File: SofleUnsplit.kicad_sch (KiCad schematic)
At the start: 117 parts, among them SW1 Switch, SW10 Switch, SW11 Switch, SW12 Switch, SW13 Switch, SW14 Switch, SW15 Switch, SW16 Switch, SW17 Switch, SW18 Switch, SW19 Switch, SW2 Switch, SW20 Switch, SW21 Switch, SW22 Switch, SW23 Switch, SW24 Switch, SW25 Switch, SW26 Switch, SW27 Switch, SW28 Switch, SW29 Switch, SW3 Switch, SW30 Switch, SW31 Switch, SW32 Switch, SW33 Switch, SW34 Switch, SW35 Switch, SW36 Switch, SW37 Switch, SW38 Switch, SW39 Switch, SW4 Switch, SW40 Switch, SW41 Switch, SW42 Switch, SW43 Switch, SW44 Switch, SW45 Switch, SW46 Switch, SW47 Switch, SW48 Switch, SW49 Switch, SW5 Switch, SW50 Switch, SW51 Switch, SW52 Switch, SW53 Switch, SW54 Switch, SW55 Switch, SW56 Switch, SW57 Switch, SW58 Switch, SW6 Switch, SW7 Switch, SW8 Switch, SW9 Switch, U1 MCU_rp2040-zero

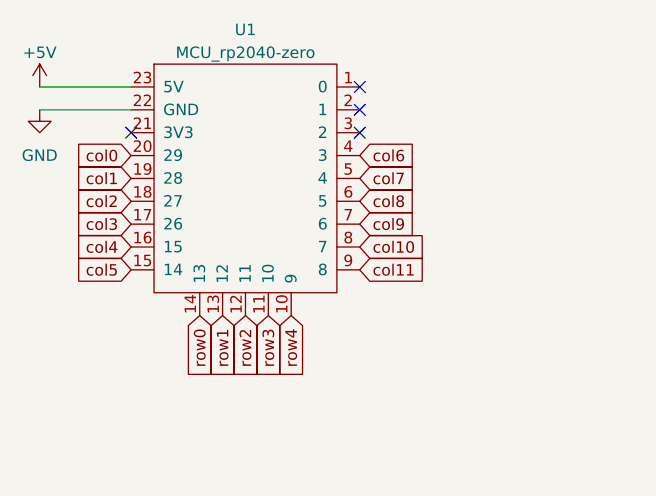
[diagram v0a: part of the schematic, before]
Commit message: Place diodes differently
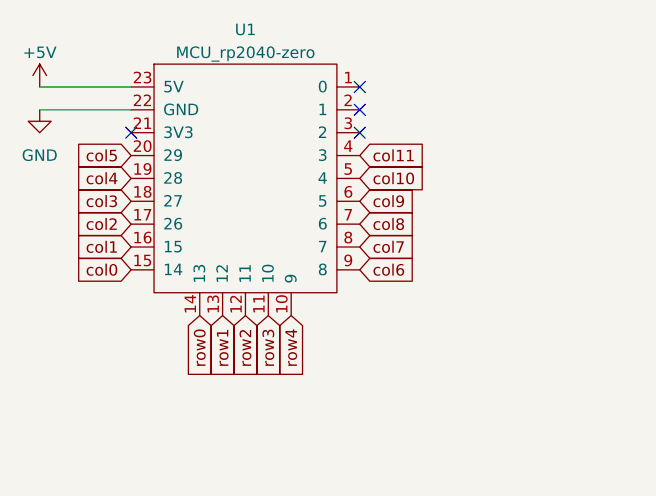
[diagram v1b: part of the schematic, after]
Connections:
- net col0: now also U1.15 (14); no longer U1.20 (29)
- net col1: now also U1.16 (15); no longer U1.19 (28)
- net col10: now also U1.5 (4); no longer U1.8 (7)
- net col11: now also U1.4 (3); no longer U1.9 (8)
- net col2: now also U1.17 (26); no longer U1.18 (27)
- net col3: now also U1.18 (27); no longer U1.17 (26)
- net col4: now also U1.19 (28); no longer U1.16 (15)
- net col5: now also U1.20 (29); no longer U1.15 (14)
- net col6: now also U1.9 (8); no longer U1.4 (3)
- net col7: now also U1.8 (7); no longer U1.5 (4)
- net col8: now also U1.7 (6); no longer U1.6 (5)
- net col9: now also U1.6 (5); no longer U1.7 (6)
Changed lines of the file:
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@@
     (stroke (width 0) (type default))
   )
-  (global_label "col8" (shape input) (at 66.04 55.88 0) (fields_autoplaced)
+  (global_label "col8" (shape input) (at 66.04 58.42 0) (fields_autoplaced)
     (effects (font (size 1.27 1.27)) (justify left))
-    (property "Intersheetrefs" "${INTERSHEET_REFS}" (at 73.0581 55.88 0)
+    (property "Intersheetrefs" "${INTERSHEET_REFS}" (at 73.0581 58.42 0)
       (effects (font (size 1.27 1.27)) (justify left) hide)
     )
@@
     )
   )
-  (global_label "col4" (shape input) (at 40.64 60.96 180) (fields_autoplaced)
+  (global_label "col4" (shape input) (at 40.64 53.34 180) (fields_autoplaced)
     (effects (font (size 1.27 1.27)) (justify right))
-    (property "Intersheetrefs" "${INTERSHEET_REFS}" (at 33.6219 60.96 0)
+    (property "Intersheetrefs" "${INTERSHEET_REFS}" (at 33.6219 53.34 0)
       (effects (font (size 1.27 1.27)) (justify right) hide)
     )
@@
     )
   )
-  (global_label "col9" (shape input) (at 66.04 58.42 0) (fields_autoplaced)
+  (global_label "col9" (shape input) (at 66.04 55.88 0) (fields_autoplaced)
     (effects (font (size 1.27 1.27)) (justify left))
-    (property "Intersheetrefs" "${INTERSHEET_REFS}" (at 73.0581 58.42 0)
+    (property "Intersheetrefs" "${INTERSHEET_REFS}" (at 73.0581 55.88 0)
       (effects (font (size 1.27 1.27)) (justify left) hide)
     )
   )
-  (global_label "col10" (shape input) (at 66.04 60.96 0) (fields_autoplaced)
+  (global_label "col10" (shape input) (at 66.04 53.34 0) (fields_autoplaced)
     (effects (font (size 1.27 1.27)) (justify left))
-    (property "Intersheetrefs" "${INTERSHEET_REFS}" (at 73.0581 60.96 0)
+    (property "Intersheetrefs" "${INTERSHEET_REFS}" (at 73.0581 53.34 0)
       (effects (font (size 1.27 1.27)) (justify left) hide)
     )
@@
     )
   )
-  (global_label "col2" (shape input) (at 40.64 55.88 180) (fields_autoplaced)
+  (global_label "col2" (shape input) (at 40.64 58.42 180) (fields_autoplaced)
+    (effects (font (size 1.27 1.27)) (justify right))
+    (property "Intersheetrefs" "${INTERSHEET_REFS}" (at 33.6219 58.42 0)
+      (effects (font (size 1.27 1.27)) (justify right) hide)
+    )
+  )
+  (global_label "col3" (shape input) (at 40.64 55.88 180) (fields_autoplaced)
     (effects (font (size 1.27 1.27)) (justify right))
     (property "Intersheetrefs" "${INTERSHEET_REFS}" (at 33.6219 55.88 0)
@@
     )
   )
-  (global_label "col3" (shape input) (at 40.64 58.42 180) (fields_autoplaced)
+  (global_label "col1" (shape input) (at 40.64 60.96 180) (fields_autoplaced)
     (effects (font (size 1.27 1.27)) (justify right))
-    (property "Intersheetrefs" "${INTERSHEET_REFS}" (at 33.6219 58.42 0)
-      (effects (font (size 1.27 1.27)) (justify right) hide)
-    )
-  )
-  (global_label "col1" (shape input) (at 40.64 53.34 180) (fields_autoplaced)
-    (effects (font (size 1.27 1.27)) (justify right))
-    (property "Intersheetrefs" "${INTERSHEET_REFS}" (at 33.6219 53.34 0)
+    (property "Intersheetrefs" "${INTERSHEET_REFS}" (at 33.6219 60.96 0)
       (effects (font (size 1.27 1.27)) (justify right) hide)
     )
@@
     )
   )
-  (global_label "col0" (shape input) (at 40.64 50.8 180) (fields_autoplaced)
+  (global_label "col0" (shape input) (at 40.64 63.5 180) (fields_autoplaced)
+    (effects (font (size 1.27 1.27)) (justify right))
+    (property "Intersheetrefs" "${INTERSHEET_REFS}" (at 33.6219 63.5 0)
+      (effects (font (size 1.27 1.27)) (justify right) hide)
+    )
+  )
+  (global_label "col5" (shape input) (at 40.64 50.8 180) (fields_autoplaced)
     (effects (font (size 1.27 1.27)) (justify right))
     (property "Intersheetrefs" "${INTERSHEET_REFS}" (at 33.6219 50.8 0)
@@
     )
   )
-  (global_label "col5" (shape input) (at 40.64 63.5 180) (fields_autoplaced)
-    (effects (font (size 1.27 1.27)) (justify right))
-    (property "Intersheetrefs" "${INTERSHEET_REFS}" (at 33.6219 63.5 0)
-      (effects (font (size 1.27 1.27)) (justify right) hide)
-    )
-  )
-  (global_label "col11" (shape input) (at 66.04 63.5 0) (fields_autoplaced)
+  (global_label "col11" (shape input) (at 66.04 50.8 0) (fields_autoplaced)
     (effects (font (size 1.27 1.27)) (justify left))
-    (property "Intersheetrefs" "${INTERSHEET_REFS}" (at 73.0581 63.5 0)
+    (property "Intersheetrefs" "${INTERSHEET_REFS}" (at 73.0581 50.8 0)
       (effects (font (size 1.27 1.27)) (justify left) hide)
     )
@@
     )
   )
-  (global_label "col6" (shape input) (at 66.04 50.8 0)
+  (global_label "col6" (shape input) (at 66.04 63.5 0)
     (effects (font (size 1.27 1.27)) (justify left))
-    (property "Intersheetrefs" "${INTERSHEET_REFS}" (at 73.0581 50.8 0)
+    (property "Intersheetrefs" "${INTERSHEET_REFS}" (at 73.0581 63.5 0)
       (effects (font (size 1.27 1.27)) (justify left) hide)
     )
@@
     )
   )
-  (global_label "col7" (shape input) (at 66.04 53.34 0) (fields_autoplaced)
+  (global_label "col7" (shape input) (at 66.04 60.96 0) (fields_autoplaced)
     (effects (font (size 1.27 1.27)) (justify left))
-    (property "Intersheetrefs" "${INTERSHEET_REFS}" (at 73.0581 53.34 0)
+    (property "Intersheetrefs" "${INTERSHEET_REFS}" (at 73.0581 60.96 0)
       (effects (font (size 1.27 1.27)) (justify left) hide)
     )

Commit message: Routing done
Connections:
- net col0: now also U1.20 (29); no longer U1.15 (14)
- net col1: now also U1.19 (28); no longer U1.16 (15)
- net col2: now also U1.18 (27); no longer U1.17 (26)
- net col3: now also U1.17 (26); no longer U1.18 (27)
- net col4: now also U1.16 (15); no longer U1.19 (28)
- net col5: now also U1.15 (14); no longer U1.20 (29)
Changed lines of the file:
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@@
     )
   )
-  (global_label "col4" (shape input) (at 40.64 53.34 180) (fields_autoplaced)
+  (global_label "col4" (shape input) (at 40.64 60.96 180) (fields_autoplaced)
     (effects (font (size 1.27 1.27)) (justify right))
-    (property "Intersheetrefs" "${INTERSHEET_REFS}" (at 33.6219 53.34 0)
+    (property "Intersheetrefs" "${INTERSHEET_REFS}" (at 33.6219 60.96 0)
       (effects (font (size 1.27 1.27)) (justify right) hide)
     )
@@
     )
   )
-  (global_label "col2" (shape input) (at 40.64 58.42 180) (fields_autoplaced)
+  (global_label "col2" (shape input) (at 40.64 55.88 180) (fields_autoplaced)
+    (effects (font (size 1.27 1.27)) (justify right))
+    (property "Intersheetrefs" "${INTERSHEET_REFS}" (at 33.6219 55.88 0)
+      (effects (font (size 1.27 1.27)) (justify right) hide)
+    )
+  )
+  (global_label "col3" (shape input) (at 40.64 58.42 180) (fields_autoplaced)
     (effects (font (size 1.27 1.27)) (justify right))
     (property "Intersheetrefs" "${INTERSHEET_REFS}" (at 33.6219 58.42 0)
@@
     )
   )
-  (global_label "col3" (shape input) (at 40.64 55.88 180) (fields_autoplaced)
+  (global_label "col1" (shape input) (at 40.64 53.34 180) (fields_autoplaced)
     (effects (font (size 1.27 1.27)) (justify right))
-    (property "Intersheetrefs" "${INTERSHEET_REFS}" (at 33.6219 55.88 0)
-      (effects (font (size 1.27 1.27)) (justify right) hide)
-    )
-  )
-  (global_label "col1" (shape input) (at 40.64 60.96 180) (fields_autoplaced)
-    (effects (font (size 1.27 1.27)) (justify right))
-    (property "Intersheetrefs" "${INTERSHEET_REFS}" (at 33.6219 60.96 0)
+    (property "Intersheetrefs" "${INTERSHEET_REFS}" (at 33.6219 53.34 0)
       (effects (font (size 1.27 1.27)) (justify right) hide)
     )
@@
     )
   )
-  (global_label "col0" (shape input) (at 40.64 63.5 180) (fields_autoplaced)
+  (global_label "col0" (shape input) (at 40.64 50.8 180) (fields_autoplaced)
+    (effects (font (size 1.27 1.27)) (justify right))
+    (property "Intersheetrefs" "${INTERSHEET_REFS}" (at 33.6219 50.8 0)
+      (effects (font (size 1.27 1.27)) (justify right) hide)
+    )
+  )
+  (global_label "col5" (shape input) (at 40.64 63.5 180) (fields_autoplaced)
     (effects (font (size 1.27 1.27)) (justify right))
     (property "Intersheetrefs" "${INTERSHEET_REFS}" (at 33.6219 63.5 0)
       (effects (font (size 1.27 1.27)) (justify right) hide)
     )
-  )
-  (global_label "col5" (shape input) (at 40.64 50.8 180) (fields_autoplaced)
-    (effects (font (size 1.27 1.27)) (justify right))
-    (property "Intersheetrefs" "${INTERSHEET_REFS}" (at 33.6219 50.8 0)
-      (effects (font (size 1.27 1.27)) (justify right) hide)
-    )

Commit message: Polishing, finishing
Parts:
- added J1: Conn_01x04, Connector_PinSocket_2.54mm:PinSocket_1x04_P2.54mm_Vertical, symbol Connector_Generic:Conn_01x04
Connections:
- net +5V: now also J1.1 (Pin_1)
- net GND: now also J1.4 (Pin_4)
- net SDA: now reaches U1.1 (0)
- net SDA: now also J1.3 (Pin_3)
- net SCL: now reaches U1.2 (1)
- net SCL: now also J1.2 (Pin_2)
- no-connect marks 4 -> 2
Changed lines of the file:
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@@
   (junction (at 326.39 191.77) (diameter 0) (color 0 0 0 0)
   )
-  (no_connect (at 66.04 43.18))
   (no_connect (at 40.64 48.26))
   (no_connect (at 66.04 48.26))
-  (no_connect (at 66.04 45.72))
   (wire (pts (xy 43.18 208.28) (xy 67.31 208.28))
     (stroke (width 0) (type default))
@@
     (stroke (width 0) (type default))
   )
+  (wire (pts (xy 113.03 41.91) (xy 121.92 41.91))
+    (stroke (width 0) (type default))
+  )
   (wire (pts (xy 96.52 208.28) (xy 124.46 208.28))
     (stroke (width 0) (type default))
@@
     (stroke (width 0) (type default))
   )
+  (wire (pts (xy 113.03 49.53) (xy 125.73 49.53))
+    (stroke (width 0) (type default))
+  )
   (wire (pts (xy 251.46 167.64) (xy 251.46 184.15))
     (stroke (width 0) (type default))
@@
     )
   )
+  (global_label "SCL" (shape input) (at 66.04 45.72 0) (fields_autoplaced)
+    (effects (font (size 1.27 1.27)) (justify left))
+    (property "Intersheetrefs" "${INTERSHEET_REFS}" (at 72.4534 45.72 0)
+      (effects (font (size 1.27 1.27)) (justify left) hide)
+    )
+  )
   (global_label "col4" (shape input) (at 166.37 157.48 90) (fields_autoplaced)
     (effects (font (size 1.27 1.27)) (justify left))
@@
     )
   )
+  (global_label "SDA" (shape input) (at 66.04 43.18 0) (fields_autoplaced)
+    (effects (font (size 1.27 1.27)) (justify left))
+    (property "Intersheetrefs" "${INTERSHEET_REFS}" (at 72.5139 43.18 0)
+      (effects (font (size 1.27 1.27)) (justify left) hide)
+    )
+  )
   (global_label "col5" (shape input) (at 195.58 157.48 90) (fields_autoplaced)
     (effects (font (size 1.27 1.27)) (justify left))
@@
     )
   )
+  (global_label "SDA" (shape input) (at 113.03 44.45 0) (fields_autoplaced)
+    (effects (font (size 1.27 1.27)) (justify left))
+    (property "Intersheetrefs" "${INTERSHEET_REFS}" (at 119.5039 44.45 0)
+      (effects (font (size 1.27 1.27)) (justify left) hide)
+    )
+  )
+  (global_label "SCL" (shape input) (at 113.03 46.99 0) (fields_autoplaced)
+    (effects (font (size 1.27 1.27)) (justify left))
+    (property "Intersheetrefs" "${INTERSHEET_REFS}" (at 119.4434 46.99 0)
+      (effects (font (size 1.27 1.27)) (justify left) hide)
+    )
+  )
   (global_label "col1" (shape input) (at 81.28 157.48 90) (fields_autoplaced)
     (effects (font (size 1.27 1.27)) (justify left))
@@
     )
   )
+  (symbol (lib_id "power:+5V") (at 125.73 49.53 0) (unit 1)
+    (in_bom yes) (on_board yes) (dnp no) (fields_autoplaced)
+    (property "Reference" "#PWR03" (at 125.73 53.34 0)
+      (effects (font (size 1.27 1.27)) hide)
+    )
+    (property "Value" "+5V" (at 125.73 45.72 0)
+      (effects (font (size 1.27 1.27)))
+    )
+    (property "Footprint" "" (at 125.73 49.53 0)
+      (effects (font (size 1.27 1.27)) hide)
+    )
+    (property "Datasheet" "" (at 125.73 49.53 0)
+      (effects (font (size 1.27 1.27)) hide)
+    )
+    (pin "1")
+    (instances
+      (project "SofleUnsplit"
+        (path "/0271784e-2195-481b-b0c9-914478a67f87"
+          (reference "#PWR03") (unit 1)
+        )
+      )
+    )
+  )
   (symbol (lib_id "Diode:1N4148W") (at 326.39 220.98 90) (unit 1)
     (in_bom yes) (on_board yes) (dnp no) (fields_autoplaced)
@@
     )
   )
+  (symbol (lib_id "Connector_Generic:Conn_01x04") (at 107.95 46.99 180) (unit 1)
+    (in_bom yes) (on_board yes) (dnp no) (fields_autoplaced)
+    (property "Reference" "J1" (at 107.95 36.83 0)
+      (effects (font (size 1.27 1.27)))
+    )
+    (property "Value" "Conn_01x04" (at 107.95 39.37 0)
+      (effects (font (size 1.27 1.27)))
+    )
+    (property "Footprint" "Connector_PinSocket_2.54mm:PinSocket_1x04_P2.54mm_Vertical" (at 107.95 46.99 0)
+      (effects (font (size 1.27 1.27)) hide)
+    )
+    (property "Datasheet" "~" (at 107.95 46.99 0)
+      (effects (font (size 1.27 1.27)) hide)
+    )
+    (pin "1")
+    (pin "2")
+    (pin "3")
+    (pin "4")
+    (instances
+      (project "SofleUnsplit"
+        (path "/0271784e-2195-481b-b0c9-914478a67f87"
+          (reference "J1") (unit 1)
+        )
+      )
+    )
+  )
   (symbol (lib_id "zzkeeb:Switch") (at 144.78 200.66 0) (unit 1)
     (in_bom yes) (on_board yes) (dnp no)
@@
         )
       )
+    )
+  )
+  (symbol (lib_id "power:GND") (at 121.92 41.91 0) (unit 1)
+    (in_bom yes) (on_board yes) (dnp no) (fields_autoplaced)
+    (property "Reference" "#PWR04" (at 121.92 48.26 0)
+      (effects (font (size 1.27 1.27)) hide)
+    )
+    (property "Value" "GND" (at 121.92 46.99 0)
+      (effects (font (size 1.27 1.27)))
+    )
+    (property "Footprint" "" (at 121.92 41.91 0)
+      (effects (font (size 1.27 1.27)) hide)
+    )
+    (property "Datasheet" "" (at 121.92 41.91 0)
+      (effects (font (size 1.27 1.27)) hide)
+    )
+    (pin "1")
+    (instances
+      (project "SofleUnsplit"
+        (path "/0271784e-2195-481b-b0c9-914478a67f87"
+          (reference "#PWR04") (unit 1)
+        )
+      )

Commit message: Finalising
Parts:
- removed J1: Conn_01x04, Connector_PinSocket_2.54mm:PinSocket_1x04_P2.54mm_Vertical, symbol Connector_Generic:Conn_01x04
- added J1: Conn_01x05, Connector_PinSocket_2.54mm:PinSocket_1x05_P2.54mm_Vertical, symbol Connector_Generic:Conn_01x05
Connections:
- net GND: now also J1.5 (Pin_5)
- net +3.3V: now reaches U1.21 (3V3)
- net +3.3V: now also J1.1 (Pin_1)
- net GP2: now reaches U1.3 (2)
- net GP2: now also J1.2 (Pin_2)
- net +5V: no longer names the net of U1.23 (5V)
- net SCL renamed GP1
- net GP1: now also J1.3 (Pin_3)
- net SDA renamed GP0
- net GP0: now also J1.4 (Pin_4)
- no-connect marks 2 -> 1
